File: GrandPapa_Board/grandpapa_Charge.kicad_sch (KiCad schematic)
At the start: 22 parts, among them J1 3.7V LiPo Single Cell, U3 MCP73871T-1CCI/ML, U4 INA180

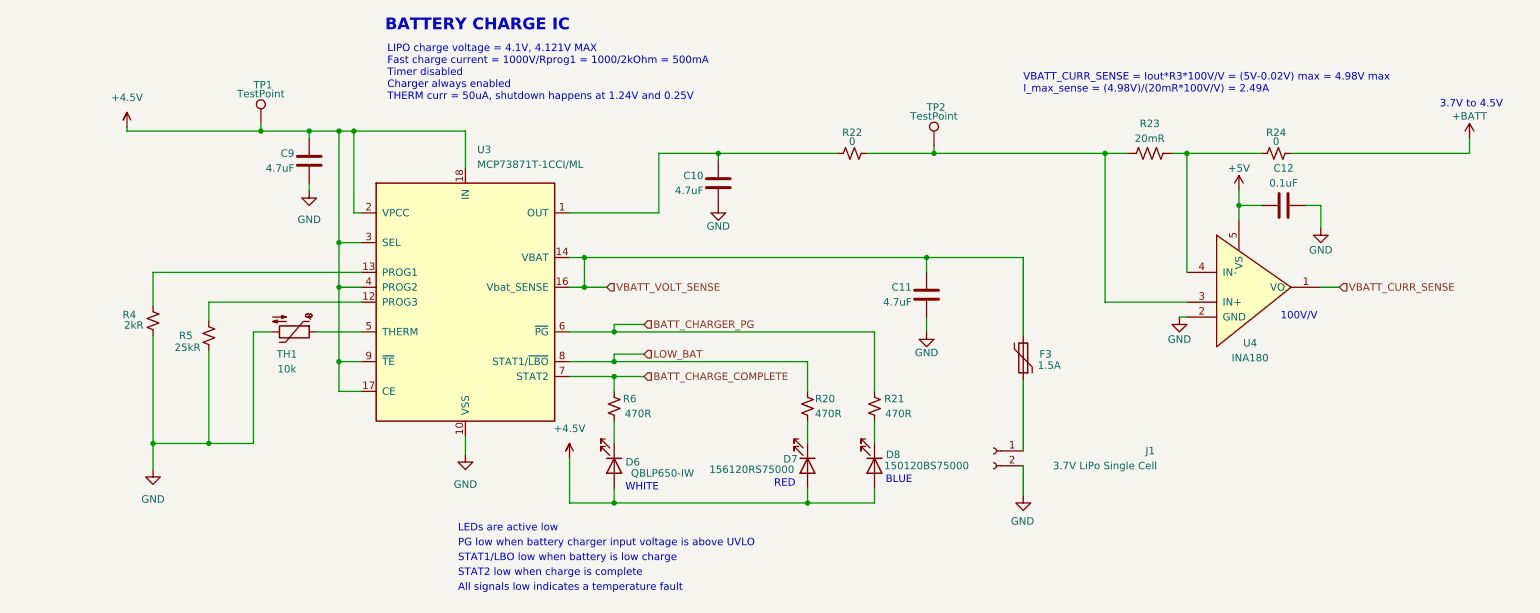
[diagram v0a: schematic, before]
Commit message: Add R28 to fix thermal shdn; Add BOM and thermistor calc sheets
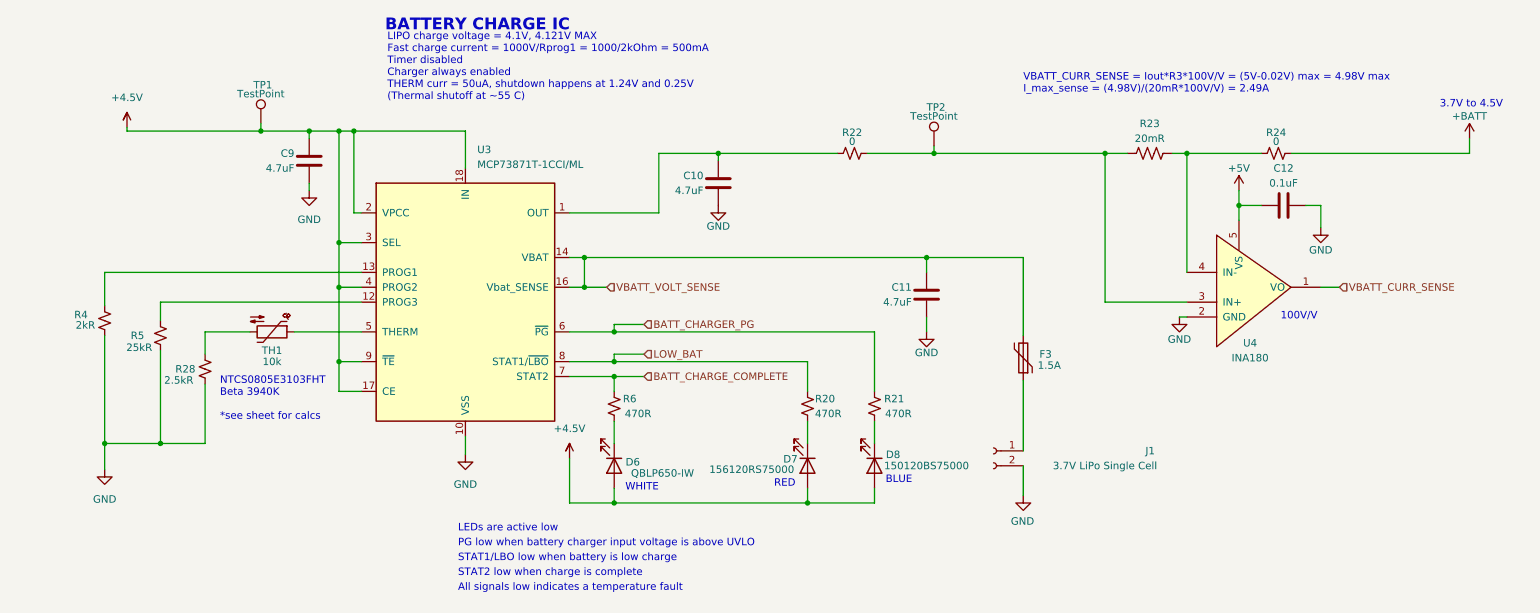
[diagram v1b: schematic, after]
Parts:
- added R28: 2.5kR, Resistor_SMD:R_0805_2012Metric_Pad1.20x1.40mm_HandSolder, symbol Device:R_Small_US
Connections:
- net GND: now also R28.2; no longer TH1.2
- new net: R28.1, TH1.2
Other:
- note added: "LIPO charge voltage = 4.1V, 4.121V MAX Fast charge current = 1000V/Rprog1 = 1000/2kOhm = 500mA Timer disabled Charger always enabled THERM curr = 50uA, shutdown happens at 1.24V and 0.25V (Thermal shutoff at ~55 C)"
- note added: "NTCS0805E3103FHT Beta 3940K *see sheet for calcs"
- note removed: "LIPO charge voltage = 4.1V, 4.121V MAX Fast charge current = 1000V/Rprog1 = 1000/2kOhm = 500mA Timer disabled Charger always enabled THERM curr = 50uA, shutdown happens at 1.24V and 0.25V"
- moved on the sheet: R4, R5, TH1
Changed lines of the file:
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@@
   (junction (at 73.66 66.04) (diameter 0) (color 0 0 0 0)
   )
-  (junction (at 48.895 119.38) (diameter 0) (color 0 0 0 0)
+  (junction (at 40.64 119.38) (diameter 0) (color 0 0 0 0)
   )
   (junction (at 118.11 100.33) (diameter 0) (color 0 0 0 0)
@@
   (junction (at 151.13 129.54) (diameter 0) (color 0 0 0 0)
   )
-  (junction (at 39.37 119.38) (diameter 0) (color 0 0 0 0)
+  (junction (at 31.115 119.38) (diameter 0) (color 0 0 0 0)
   )
   (junction (at 113.03 87.63) (diameter 0) (color 0 0 0 0)
@@
     (stroke (width 0) (type default) (color 0 0 0 0))
   )
-  (wire (pts (xy 39.37 100.965) (xy 39.37 119.38))
+  (wire (pts (xy 31.115 100.965) (xy 31.115 119.38))
     (stroke (width 0) (type default) (color 0 0 0 0))
   )
@@
     (stroke (width 0) (type default) (color 0 0 0 0))
   )
-  (wire (pts (xy 39.37 90.17) (xy 39.37 95.885))
+  (wire (pts (xy 31.115 90.17) (xy 31.115 95.885))
     (stroke (width 0) (type default) (color 0 0 0 0))
   )
@@
     (stroke (width 0) (type default) (color 0 0 0 0))
   )
-  (wire (pts (xy 56.515 100.33) (xy 59.69 100.33))
+  (wire (pts (xy 48.26 100.33) (xy 55.88 100.33))
     (stroke (width 0) (type default) (color 0 0 0 0))
   )
@@
     (stroke (width 0) (type default) (color 0 0 0 0))
   )
-  (wire (pts (xy 48.895 95.25) (xy 74.93 95.25))
-    (stroke (width 0) (type default) (color 0 0 0 0))
-  )
-  (wire (pts (xy 67.31 100.33) (xy 74.93 100.33))
+  (wire (pts (xy 40.64 95.25) (xy 74.93 95.25))
+    (stroke (width 0) (type default) (color 0 0 0 0))
+  )
+  (wire (pts (xy 63.5 100.33) (xy 74.93 100.33))
     (stroke (width 0) (type default) (color 0 0 0 0))
   )
@@
     (stroke (width 0) (type default) (color 0 0 0 0))
   )
-  (wire (pts (xy 39.37 119.38) (xy 48.895 119.38))
+  (wire (pts (xy 31.115 119.38) (xy 40.64 119.38))
     (stroke (width 0) (type default) (color 0 0 0 0))
   )
@@
     (stroke (width 0) (type default) (color 0 0 0 0))
   )
-  (wire (pts (xy 39.37 123.825) (xy 39.37 119.38))
+  (wire (pts (xy 31.115 123.825) (xy 31.115 119.38))
     (stroke (width 0) (type default) (color 0 0 0 0))
   )
@@
     (stroke (width 0) (type default) (color 0 0 0 0))
   )
-  (wire (pts (xy 48.895 95.25) (xy 48.895 98.425))
-    (stroke (width 0) (type default) (color 0 0 0 0))
-  )
-  (wire (pts (xy 56.515 100.33) (xy 56.515 119.38))
+  (wire (pts (xy 48.26 109.22) (xy 48.26 119.38))
+    (stroke (width 0) (type default) (color 0 0 0 0))
+  )
+  (wire (pts (xy 40.64 95.25) (xy 40.64 98.425))
+    (stroke (width 0) (type default) (color 0 0 0 0))
+  )
+  (wire (pts (xy 48.26 100.33) (xy 48.26 104.14))
     (stroke (width 0) (type default) (color 0 0 0 0))
   )
@@
     (stroke (width 0) (type default) (color 0 0 0 0))
   )
-  (wire (pts (xy 48.895 103.505) (xy 48.895 119.38))
+  (wire (pts (xy 40.64 103.505) (xy 40.64 119.38))
     (stroke (width 0) (type default) (color 0 0 0 0))
   )
@@
     (stroke (width 0) (type default) (color 0 0 0 0))
   )
-  (wire (pts (xy 48.895 119.38) (xy 56.515 119.38))
+  (wire (pts (xy 40.64 119.38) (xy 48.26 119.38))
     (stroke (width 0) (type default) (color 0 0 0 0))
   )
@@
     (stroke (width 0) (type default) (color 0 0 0 0))
   )
-  (wire (pts (xy 39.37 90.17) (xy 74.93 90.17))
+  (wire (pts (xy 31.115 90.17) (xy 74.93 90.17))
     (stroke (width 0) (type default) (color 0 0 0 0))
   )
@@
   )
   (text "All signals low indicates a temperature fault\n" (at 91.44 144.78 0)
+    (effects (font (size 1.27 1.27)) (justify left bottom))
+  )
+  (text "NTCS0805E3103FHT\nBeta 3940K\n\n*see sheet for calcs" (at 50.8 115.57 0)
     (effects (font (size 1.27 1.27)) (justify left bottom))
   )
@@
     (effects (font (size 1.27 1.27)) (justify left bottom))
   )
-  (text "LIPO charge voltage = 4.1V, 4.121V MAX\nFast charge current = 1000V/Rprog1 = 1000/2kOhm = 500mA\nTimer disabled\nCharger always enabled\nTHERM curr = 50uA, shutdown happens at 1.24V and 0.25V\n"
+  (text "LIPO charge voltage = 4.1V, 4.121V MAX\nFast charge current = 1000V/Rprog1 = 1000/2kOhm = 500mA\nTimer disabled\nCharger always enabled\nTHERM curr = 50uA, shutdown happens at 1.24V and 0.25V\n(Thermal shutoff at ~55 C)"
     (at 79.375 60.96 0)
     (effects (font (size 1.27 1.27)) (justify left bottom))
@@
     (pin "2")
   )
-  (symbol (lib_id "power:GND") (at 39.37 123.825 0) (unit 1)
+  (symbol (lib_id "power:GND") (at 31.115 123.825 0) (unit 1)
     (in_bom yes) (on_board yes) (fields_autoplaced)
-    (property "Reference" "#PWR016" (id 0) (at 39.37 130.175 0)
-      (effects (font (size 1.27 1.27)) hide)
-    )
-    (property "Value" "GND" (id 1) (at 39.37 128.905 0))
-    (property "Footprint" "" (id 2) (at 39.37 123.825 0)
-      (effects (font (size 1.27 1.27)) hide)
-    )
-    (property "Datasheet" "" (id 3) (at 39.37 123.825 0)
-      (effects (font (size 1.27 1.27)) hide)
-    )
-    (pin "1")
-  )
-  (symbol (lib_id "Device:R_Small_US") (at 48.895 100.965 0) (unit 1)
-    (in_bom yes) (on_board yes)
-    (property "Reference" "R5" (id 0) (at 43.815 100.965 0)
-      (effects (font (size 1.27 1.27)) (justify left))
-    )
-    (property "Value" "25kR" (id 1) (at 43.053 102.997 0)
-      (effects (font (size 1.27 1.27)) (justify left))
-    )
-    (property "Footprint" "Resistor_SMD:R_0805_2012Metric_Pad1.20x1.40mm_HandSolder" (id 2) (at 48.895 100.965 0)
-      (effects (font (size 1.27 1.27)) hide)
-    )
-    (property "Datasheet" "~" (id 3) (at 48.895 100.965 0)
+    (property "Reference" "#PWR016" (id 0) (at 31.115 130.175 0)
+      (effects (font (size 1.27 1.27)) hide)
+    )
+    (property "Value" "GND" (id 1) (at 31.115 128.905 0))
+    (property "Footprint" "" (id 2) (at 31.115 123.825 0)
+      (effects (font (size 1.27 1.27)) hide)
+    )
+    (property "Datasheet" "" (id 3) (at 31.115 123.825 0)
+      (effects (font (size 1.27 1.27)) hide)
+    )
+    (pin "1")
+  )
+  (symbol (lib_id "Device:R_Small_US") (at 40.64 100.965 0) (unit 1)
+    (in_bom yes) (on_board yes)
+    (property "Reference" "R5" (id 0) (at 35.56 100.965 0)
+      (effects (font (size 1.27 1.27)) (justify left))
+    )
+    (property "Value" "25kR" (id 1) (at 34.798 102.997 0)
+      (effects (font (size 1.27 1.27)) (justify left))
+    )
+    (property "Footprint" "Resistor_SMD:R_0805_2012Metric_Pad1.20x1.40mm_HandSolder" (id 2) (at 40.64 100.965 0)
+      (effects (font (size 1.27 1.27)) hide)
+    )
+    (property "Datasheet" "~" (id 3) (at 40.64 100.965 0)
       (effects (font (size 1.27 1.27)) hide)
     )
@@
     (pin "2")
   )
+  (symbol (lib_id "Device:R_Small_US") (at 48.26 106.68 0) (unit 1)
+    (in_bom yes) (on_board yes)
+    (property "Reference" "R28" (id 0) (at 43.18 106.68 0)
+      (effects (font (size 1.27 1.27)) (justify left))
+    )
+    (property "Value" "2.5kR" (id 1) (at 41.275 108.585 0)
+      (effects (font (size 1.27 1.27)) (justify left))
+    )
+    (property "Footprint" "Resistor_SMD:R_0805_2012Metric_Pad1.20x1.40mm_HandSolder" (id 2) (at 48.26 106.68 0)
+      (effects (font (size 1.27 1.27)) hide)
+    )
+    (property "Datasheet" "~" (id 3) (at 48.26 106.68 0)
+      (effects (font (size 1.27 1.27)) hide)
+    )
+    (pin "1")
+    (pin "2")
+  )
   (symbol (lib_id "Device:R_Small_US") (at 151.13 113.03 0) (unit 1)
     (in_bom yes) (on_board yes)
@@
     (pin "2")
   )
-  (symbol (lib_id "Device:R_Small_US") (at 39.37 98.425 0) (unit 1)
-    (in_bom yes) (on_board yes)
-    (property "Reference" "R4" (id 0) (at 34.163 97.409 0)
-      (effects (font (size 1.27 1.27)) (justify left))
-    )
-    (property "Value" "2kR" (id 1) (at 34.417 99.187 0)
-      (effects (font (size 1.27 1.27)) (justify left))
-    )
-    (property "Footprint" "Resistor_SMD:R_0805_2012Metric_Pad1.20x1.40mm_HandSolder" (id 2) (at 39.37 98.425 0)
-      (effects (font (size 1.27 1.27)) hide)
-    )
-    (property "Datasheet" "~" (id 3) (at 39.37 98.425 0)
+  (symbol (lib_id "Device:R_Small_US") (at 31.115 98.425 0) (unit 1)
+    (in_bom yes) (on_board yes)
+    (property "Reference" "R4" (id 0) (at 25.908 97.409 0)
+      (effects (font (size 1.27 1.27)) (justify left))
+    )
+    (property "Value" "2kR" (id 1) (at 26.162 99.187 0)
+      (effects (font (size 1.27 1.27)) (justify left))
+    )
+    (property "Footprint" "Resistor_SMD:R_0805_2012Metric_Pad1.20x1.40mm_HandSolder" (id 2) (at 31.115 98.425 0)
+      (effects (font (size 1.27 1.27)) hide)
+    )
+    (property "Datasheet" "~" (id 3) (at 31.115 98.425 0)
       (effects (font (size 1.27 1.27)) hide)
     )
@@
     (pin "1")
   )
-  (symbol (lib_id "Device:Thermistor_NTC") (at 63.5 100.33 270) (unit 1)
-    (in_bom yes) (on_board yes)
-    (property "Reference" "TH1" (id 0) (at 62.23 104.14 90))
-    (property "Value" "10k" (id 1) (at 62.23 106.68 90))
-    (property "Footprint" "Resistor_SMD:R_0805_2012Metric_Pad1.20x1.40mm_HandSolder" (id 2) (at 64.77 100.33 0)
-      (effects (font (size 1.27 1.27)) hide)
-    )
-    (property "Datasheet" "~" (id 3) (at 64.77 100.33 0)
-      (effects (font (size 1.27 1.27)) hide)
-    )
+  (symbol (lib_id "Device:Thermistor_NTC") (at 59.69 100.33 270) (unit 1)
+    (in_bom yes) (on_board yes)
+    (property "Reference" "TH1" (id 0) (at 59.69 103.505 90))
+    (property "Value" "10k" (id 1) (at 59.69 105.41 90))
+    (property "Footprint" "Resistor_SMD:R_0805_2012Metric_Pad1.20x1.40mm_HandSolder" (id 2) (at 60.96 100.33 0)
+      (effects (font (size 1.27 1.27)) hide)
+    )
+    (property "Datasheet" "~" (id 3) (at 60.96 100.33 0)
+      (effects (font (size 1.27 1.27)) hide)
+    )

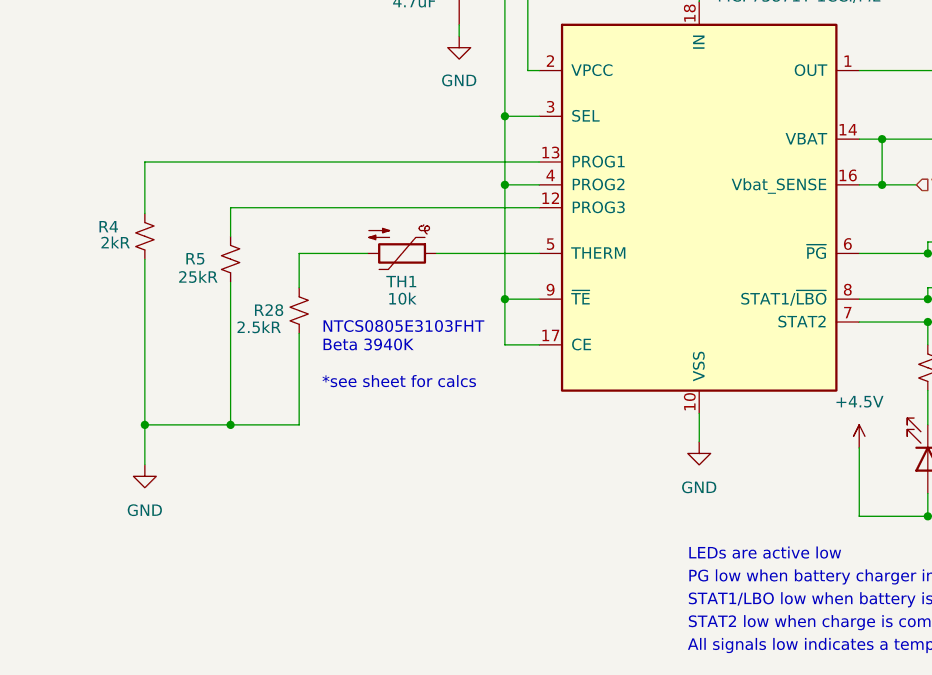
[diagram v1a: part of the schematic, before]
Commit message: Add jumper to bypass thermal shutdown
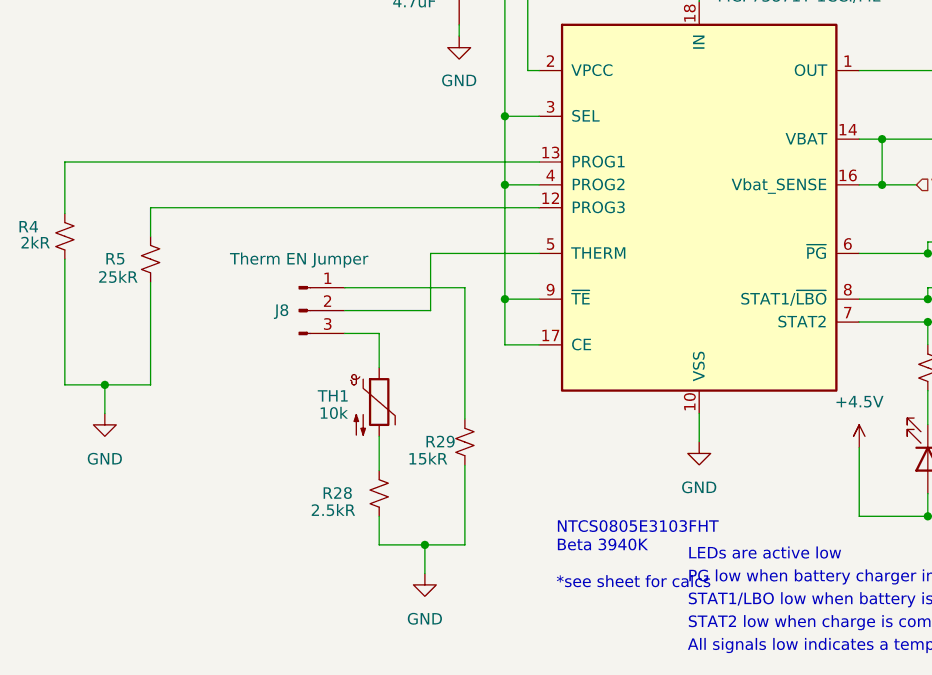
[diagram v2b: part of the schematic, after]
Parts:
- added J8: Therm EN Jumper, Connector_PinHeader_2.54mm:PinHeader_1x03_P2.54mm_Vertical, symbol Connector:Conn_01x03_Male
- added R29: 15kR, Resistor_SMD:R_0805_2012Metric_Pad1.20x1.40mm_HandSolder, symbol Device:R_Small_US
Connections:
- net GND: now also R29.2
- net at U3.5 (THERM): now also J8.2 (Pin_2); no longer TH1.1
- new net: J8.1 (Pin_1), R29.1
- new net: J8.3 (Pin_3), TH1.1
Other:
- moved on the sheet: R28, R4, R5, TH1

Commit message: minor PCB changes, fix logger mounting hole placement, minor schematic cleanup
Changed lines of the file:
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@@
     (effects (font (size 1.27 1.27)) (justify left bottom))
   )
-  (text "All signals low indicates a temperature fault\n" (at 91.44 144.78 0)
+  (text "All signals low indicates a temperature fault\n" (at 110.49 146.05 0)
     (effects (font (size 1.27 1.27)) (justify left bottom))
   )
@@
     (effects (font (size 1.27 1.27)) (justify left bottom))
   )
-  (text "STAT1/LBO low when battery is low charge" (at 91.44 139.7 0)
+  (text "STAT1/LBO low when battery is low charge" (at 110.49 140.97 0)
     (effects (font (size 1.27 1.27)) (justify left bottom))
   )
@@
     (effects (font (size 1.27 1.27)) (justify left bottom))
   )
-  (text "STAT2 low when charge is complete" (at 91.44 142.24 0)
+  (text "STAT2 low when charge is complete" (at 110.49 143.51 0)
     (effects (font (size 1.27 1.27)) (justify left bottom))
   )
-  (text "LEDs are active low\n" (at 91.44 134.62 0)
+  (text "LEDs are active low\n" (at 110.49 135.89 0)
     (effects (font (size 1.27 1.27)) (justify left bottom))
   )
@@
   )
   (text "PG low when battery charger input voltage is above UVLO"
-    (at 91.44 137.16 0)
+    (at 110.49 138.43 0)
     (effects (font (size 1.27 1.27)) (justify left bottom))
   )

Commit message: Address Jack's comments, minor schematic text cleanup
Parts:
- R29: value 15kR -> 10kR
- R4: value 2kR -> 10kR
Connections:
- net BATT_CHARGER_PG renamed BATT_CHARGER_PG_L
- net BATT_CHARGE_COMPLETE renamed BATT_CHARGE_COMPLETE_L
- net LOW_BAT renamed LOW_BAT_L
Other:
- note added: "Beta 3940K"
- note added: "LIPO charge voltage = 4.1V, 4.121V MAX Fast charge current = 1000V/Rprog1 = 1000/2kOhm = 500mA Timer disabled Charger always enabled THERM curr = 50uA, shutdown happens at 1.24V and 0.25V (Thermal shutoff at ~55 C, see NTC RT Calculations Excel sheet in project Github folder)"
- note added: "NTCS0805E3103FHT"
- note removed: "LIPO charge voltage = 4.1V, 4.121V MAX Fast charge current = 1000V/Rprog1 = 1000/2kOhm = 500mA Timer disabled Charger always enabled THERM curr = 50uA, shutdown happens at 1.24V and 0.25V (Thermal shutoff at ~55 C)"
- note removed: "NTCS0805E3103FHT Beta 3940K *see sheet for calcs"
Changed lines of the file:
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@@
     (effects (font (size 1.27 1.27)) (justify left bottom))
   )
-  (text "NTCS0805E3103FHT\nBeta 3940K\n\n*see sheet for calcs" (at 76.835 137.795 0)
+  (text "Beta 3940K\n\n" (at 41.91 123.19 0)
     (effects (font (size 1.27 1.27)) (justify left bottom))
   )
@@
   )
   (text "RED" (at 145.415 127 0)
+    (effects (font (size 1.27 1.27)) (justify left bottom))
+  )
+  (text "NTCS0805E3103FHT" (at 34.29 115.57 0)
     (effects (font (size 1.27 1.27)) (justify left bottom))
   )
@@
     (effects (font (size 1.27 1.27)) (justify left bottom))
   )
-  (text "LIPO charge voltage = 4.1V, 4.121V MAX\nFast charge current = 1000V/Rprog1 = 1000/2kOhm = 500mA\nTimer disabled\nCharger always enabled\nTHERM curr = 50uA, shutdown happens at 1.24V and 0.25V\n(Thermal shutoff at ~55 C)"
+  (text "LIPO charge voltage = 4.1V, 4.121V MAX\nFast charge current = 1000V/Rprog1 = 1000/2kOhm = 500mA\nTimer disabled\nCharger always enabled\nTHERM curr = 50uA, shutdown happens at 1.24V and 0.25V\n(Thermal shutoff at ~55 C, see NTC RT Calculations Excel sheet in project Github folder)"
     (at 79.375 60.96 0)
     (effects (font (size 1.27 1.27)) (justify left bottom))
@@
     (effects (font (size 1.27 1.27)) (justify left bottom))
   )
-  (hierarchical_label "LOW_BAT" (shape input) (at 123.19 104.14 0)
+  (hierarchical_label "LOW_BAT_L" (shape input) (at 123.19 104.14 0)
     (effects (font (size 1.27 1.27)) (justify left))
   )
@@
     (effects (font (size 1.27 1.27)) (justify left))
   )
-  (hierarchical_label "BATT_CHARGER_PG" (shape input) (at 123.19 99.06 0)
+  (hierarchical_label "BATT_CHARGER_PG_L" (shape input) (at 123.19 99.06 0)
     (effects (font (size 1.27 1.27)) (justify left))
   )
@@
     (effects (font (size 1.27 1.27)) (justify left))
   )
-  (hierarchical_label "BATT_CHARGE_COMPLETE" (shape input) (at 123.19 107.95 0)
+  (hierarchical_label "BATT_CHARGE_COMPLETE_L" (shape input) (at 123.19 107.95 0)
     (effects (font (size 1.27 1.27)) (justify left))
   )
@@
   (symbol (lib_id "Device:R_Small_US") (at 66.675 121.285 0) (unit 1)
     (in_bom yes) (on_board yes)
-    (property "Reference" "R29" (id 0) (at 62.23 121.285 0)
-      (effects (font (size 1.27 1.27)) (justify left))
-    )
-    (property "Value" "15kR" (id 1) (at 60.325 123.19 0)
+    (property "Reference" "R29" (id 0) (at 68.58 120.65 0)
+      (effects (font (size 1.27 1.27)) (justify left))
+    )
+    (property "Value" "10kR" (id 1) (at 68.58 123.19 0)
       (effects (font (size 1.27 1.27)) (justify left))
     )
@@
       (effects (font (size 1.27 1.27)) (justify left))
     )
-    (property "Value" "2kR" (id 1) (at 17.272 99.187 0)
-      (effects (font (size 1.27 1.27)) (justify left))
-    )
+    (property "Value" "10kR" (id 1) (at 15.24 99.06 0)
+      (effects (font (size 1.27 1.27)) (justify left))
+    )

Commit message: missed F3, update PDF
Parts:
- F3: footprint Fuse:Fuse_0805_2012Metric_Pad1.15x1.40mm_HandSolder -> Fuse:Fuse_1812_4532Metric_Pad1.30x3.40mm_HandSolder
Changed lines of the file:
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@@
     (property "Reference" "F3" (id 0) (at 191.77 104.14 0))
     (property "Value" "1.5A" (id 1) (at 192.405 106.045 0))
-    (property "Footprint" "Fuse:Fuse_0805_2012Metric_Pad1.15x1.40mm_HandSolder" (id 2) (at 186.69 99.695 0)
+    (property "Footprint" "Fuse:Fuse_1812_4532Metric_Pad1.30x3.40mm_HandSolder" (id 2) (at 186.69 99.695 0)
       (effects (font (size 1.27 1.27)) (justify left) hide)
     )
